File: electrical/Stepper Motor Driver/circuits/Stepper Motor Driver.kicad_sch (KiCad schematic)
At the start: 1 part, among them M2 Stepper_Motor_bipolar

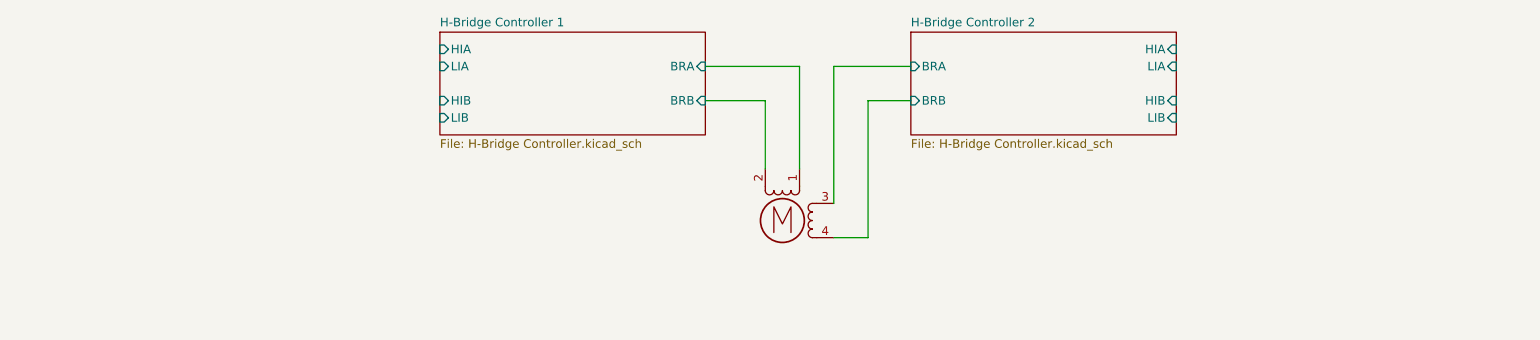
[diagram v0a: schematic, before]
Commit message: Adding low-pass input filter
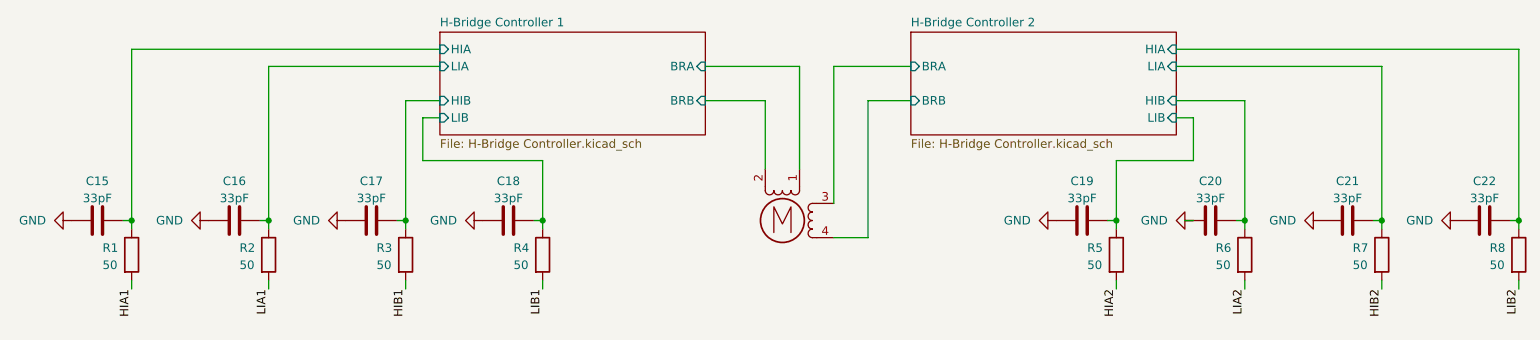
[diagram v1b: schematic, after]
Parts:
- added C15, C16, C17, C18, C19, C20, C21, C22: 33pF, symbol Device:C
- added R1, R2, R3, R4, R5, R6, R7, R8: 50, symbol Device:R
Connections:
- net H-Bridge Controller 1/HIA: now also C15.2, R1.1
- net H-Bridge Controller 1/HIB: now also C17.2, R3.1
- net H-Bridge Controller 1/LIA: now also C16.2, R2.1
- net H-Bridge Controller 1/LIB: now also C18.2, R4.1
- net H-Bridge Controller 2/HIA: now also C22.2, R8.1
- net H-Bridge Controller 2/HIB: now also C20.2, R6.1
- net H-Bridge Controller 2/LIA: now also C21.2, R7.1
- net H-Bridge Controller 2/LIB: now also C19.2, R5.1
- new net GND: C15.1, C16.1, C17.1, C18.1, C19.1, C20.1, C21.1, C22.1
- new net HIA1: R1.2
- new net HIA2: R5.2
- new net HIB1: R3.2
- new net HIB2: R7.2
- new net LIA1: R2.2
- new net LIA2: R6.2
- new net LIB1: R4.2
- new net LIB2: R8.2
